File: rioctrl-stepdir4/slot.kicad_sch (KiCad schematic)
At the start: 17 parts, among them J1 Conn_02x13_Odd_Even, Q1 BSS138W, Q2 BSS138W, Q3 AO3401A, Q4 AO3401A

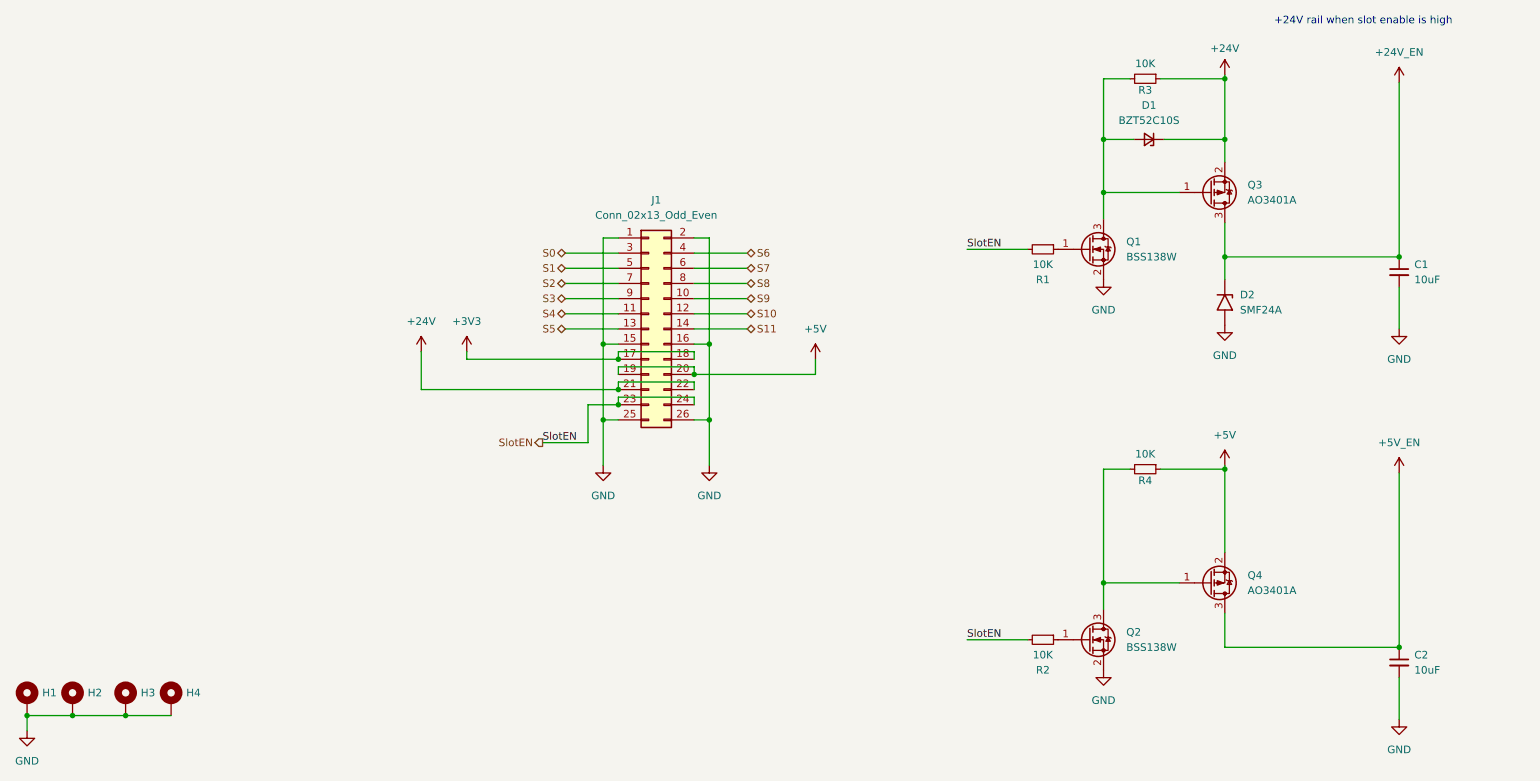
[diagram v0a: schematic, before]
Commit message: rioctrl-stepdir4: pass ERC and DRC
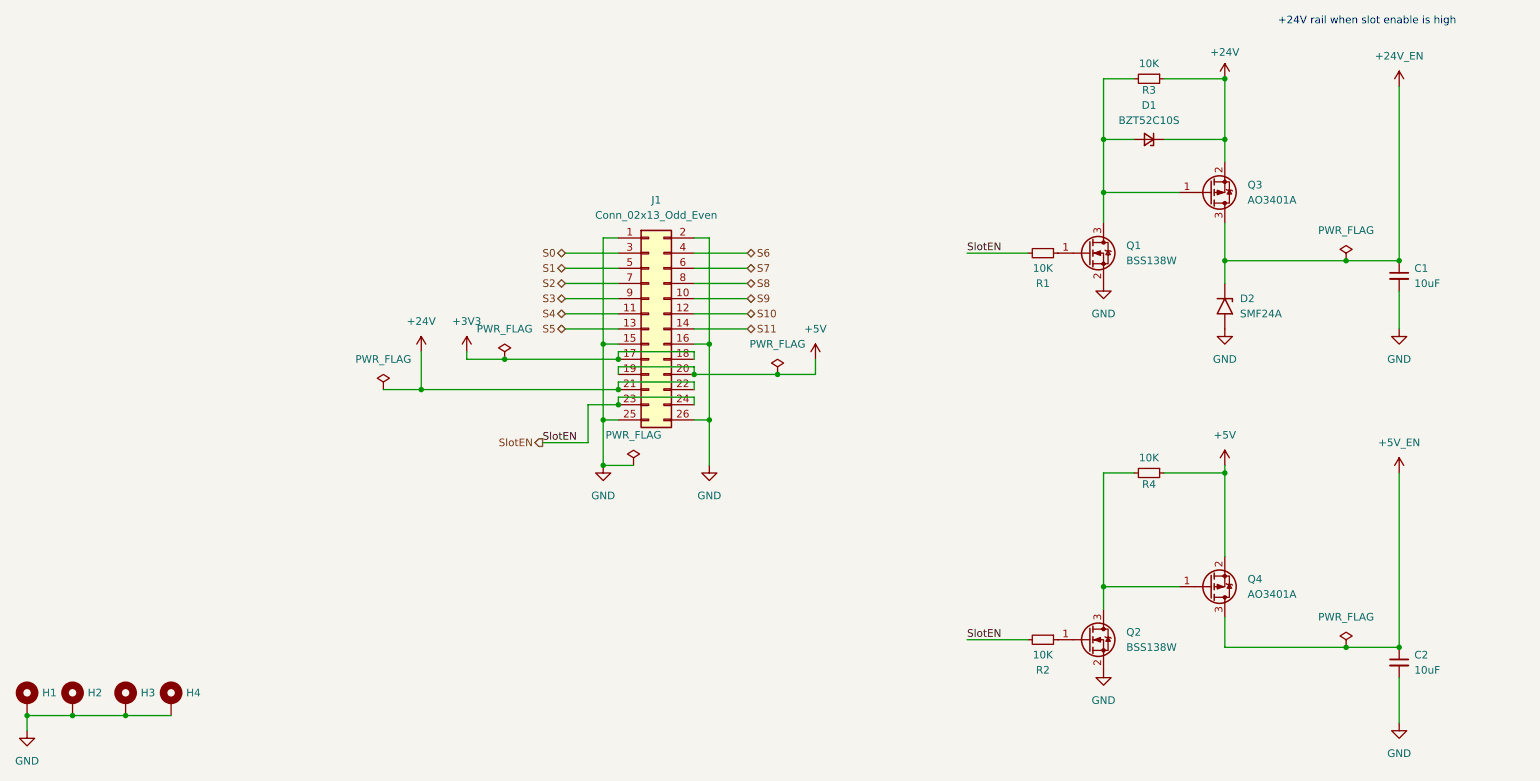
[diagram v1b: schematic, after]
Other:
- moved on the sheet: C1, D2, Q1, Q4, R1, R3, R4

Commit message: Fix ERC, add title information to sch, add initial version of build scripts
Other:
- company: (none) -> R. Veips
- title: (none) -> rioctrl-stepdir4
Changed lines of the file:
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@@
 	(generator_version "8.0")
 	(paper "A4")
+	(title_block
+		(title "rioctrl-stepdir4")
+		(date "2024-08-25")
+		(rev "${VERSION}")
+		(company "R. Veips")
+	)
 	(junction
 		(at 213.36 118.11)

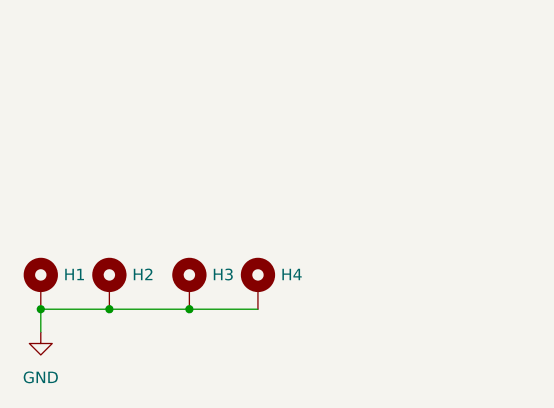
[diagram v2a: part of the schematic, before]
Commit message: Fill in BOM (LCSC#)
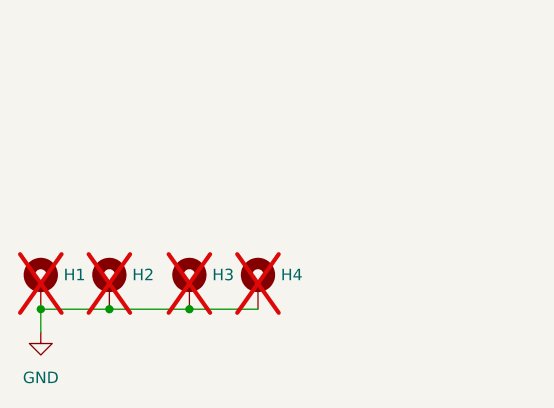
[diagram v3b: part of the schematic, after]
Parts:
- H1, H2, H3, H4: now not fitted
- J1: LCSC# (none) -> C2894993
- R1, R2, R3, R4: LCSC# (none) -> C98220
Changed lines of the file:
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@@
 		(in_bom no)
 		(on_board yes)
-		(dnp no)
+		(dnp yes)
 		(fields_autoplaced yes)
 		(property "Reference" "H4"
@@
 		(in_bom no)
 		(on_board yes)
-		(dnp no)
+		(dnp yes)
 		(fields_autoplaced yes)
 		(property "Reference" "H1"
@@
 			)
 		)
+		(property "LCSC#" "C2894993"
+			(at 137.16 74.93 0)
+			(effects
+				(font
+					(size 1.27 1.27)
+				)
+				(hide yes)
+			)
+		)
 		(pin "15"
 		)
@@
 			)
 		)
+		(property "LCSC#" "C98220"
+			(at 203.2 127 0)
+			(effects
+				(font
+					(size 1.27 1.27)
+				)
+				(hide yes)
+			)
+		)
 		(pin "1"
 		)
@@
 			)
 		)
+		(property "LCSC#" "C98220"
+			(at 220.98 33.02 0)
+			(effects
+				(font
+					(size 1.27 1.27)
+				)
+				(hide yes)
+			)
+		)
 		(pin "1"
 		)
@@
 		)
 		(property "Description" ""
+			(at 220.98 99.06 0)
+			(effects
+				(font
+					(size 1.27 1.27)
+				)
+				(hide yes)
+			)
+		)
+		(property "LCSC#" "C98220"
 			(at 220.98 99.06 0)
 			(effects
@@
 			)
 		)
+		(property "LCSC#" "C98220"
+			(at 203.2 62.23 0)
+			(effects
+				(font
+					(size 1.27 1.27)
+				)
+				(hide yes)
+			)
+		)
 		(pin "1"
 		)
@@
 		(in_bom no)
 		(on_board yes)
-		(dnp no)
+		(dnp yes)
 		(fields_autoplaced yes)
 		(property "Reference" "H3"
@@
 		(in_bom no)
 		(on_board yes)
-		(dnp no)
+		(dnp yes)
 		(fields_autoplaced yes)
 		(property "Reference" "H2"

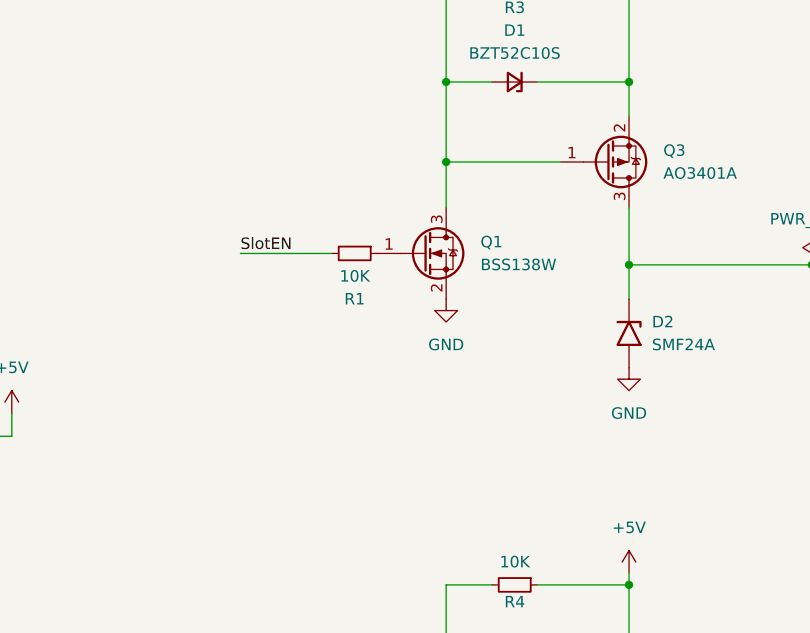
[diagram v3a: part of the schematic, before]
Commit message: Add forgotten series resistor for 24V output transistors in rioctrl-stepdir4
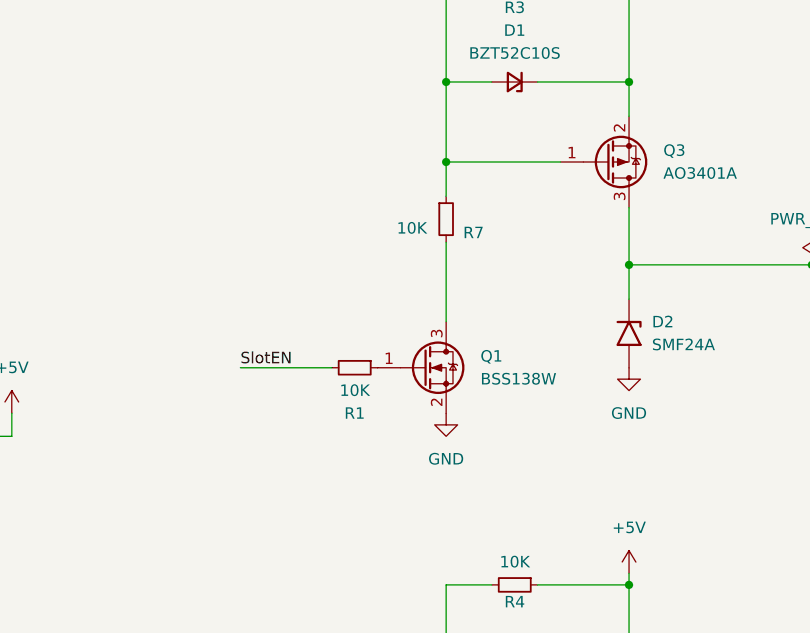
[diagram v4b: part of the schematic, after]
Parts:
- added R7: 10K, Resistor_SMD:R_0603_1608Metric, symbol Device:R_Small
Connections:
- net at D1.2 (A), Q3.1 (G), R3.2: now also R7.1; no longer Q1.3 (D)
- new net: Q1.3 (D), R7.2
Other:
- moved on the sheet: Q1, R1
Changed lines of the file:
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@@
 	(wire
 		(pts
-			(xy 190.5 62.23) (xy 200.66 62.23)
+			(xy 190.5 74.93) (xy 200.66 74.93)
 		)
 		(stroke
@@
 	(wire
 		(pts
-			(xy 213.36 52.07) (xy 213.36 57.15)
+			(xy 213.36 52.07) (xy 213.36 55.88)
 		)
 		(stroke
@@
 		(pts
 			(xy 158.75 82.55) (xy 165.1 82.55)
+		)
+		(stroke
+			(width 0)
+			(type default)
+		)
+	)
+	(wire
+		(pts
+			(xy 213.36 60.96) (xy 213.36 69.85)
 		)
 		(stroke
@@
 	)
 	(label "SlotEN"
-		(at 190.5 62.23 0)
+		(at 190.5 74.93 0)
 		(fields_autoplaced yes)
 		(effects
@@
 	(symbol
 		(lib_id "hadv-transistors:BSS138W")
-		(at 210.82 62.23 0)
+		(at 210.82 74.93 0)
 		(unit 1)
 		(exclude_from_sim no)
@@
 		(fields_autoplaced yes)
 		(property "Reference" "Q1"
-			(at 217.17 60.96 0)
+			(at 217.17 73.66 0)
 			(effects
 				(font
@@
 		)
 		(property "Value" "BSS138W"
-			(at 217.17 63.5 0)
+			(at 217.17 76.2 0)
 			(effects
 				(font
@@
 		)
 		(property "Footprint" "Package_TO_SOT_SMD:SOT-323_SC-70"
-			(at 215.9 59.69 0)
+			(at 215.9 72.39 0)
 			(effects
 				(font
@@
 		)
 		(property "Datasheet" "~"
-			(at 210.82 62.23 0)
+			(at 210.82 74.93 0)
 			(effects
 				(font
@@
 		)
 		(property "Description" ""
-			(at 210.82 62.23 0)
+			(at 210.82 74.93 0)
 			(effects
 				(font
@@
 		)
 		(property "MPN" "BSS138W"
-			(at 210.82 62.23 0)
+			(at 210.82 74.93 0)
 			(effects
 				(font
@@
 		)
 		(property "Manufacturer" "Jiangsu Changjing Electronics Technology Co., Ltd."
-			(at 210.82 62.23 0)
+			(at 210.82 74.93 0)
 			(effects
 				(font
@@
 		)
 		(property "LCSC#" "C504052"
-			(at 210.82 62.23 0)
+			(at 210.82 74.93 0)
 			(effects
 				(font
@@
 	(symbol
 		(lib_id "power:GND")
-		(at 213.36 67.31 0)
+		(at 213.36 80.01 0)
 		(unit 1)
 		(exclude_from_sim no)
@@
 		(fields_autoplaced yes)
 		(property "Reference" "#PWR06"
-			(at 213.36 73.66 0)
+			(at 213.36 86.36 0)
 			(effects
 				(font
@@
 		)
 		(property "Value" "GND"
-			(at 213.36 72.39 0)
+			(at 213.36 85.09 0)
 			(effects
 				(font
@@
 		)
 		(property "Footprint" ""
-			(at 213.36 67.31 0)
+			(at 213.36 80.01 0)
 			(effects
 				(font
@@
 		)
 		(property "Datasheet" ""
-			(at 213.36 67.31 0)
+			(at 213.36 80.01 0)
 			(effects
 				(font
@@
 		)
 		(property "Description" "Power symbol creates a global label with name \"GND\" , ground"
-			(at 213.36 67.31 0)
+			(at 213.36 80.01 0)
 			(effects
 				(font
@@
 				(path "/09587842-9628-4761-8ca3-5c7cdb77bd67/37e028e8-dcad-4a75-b244-5f607e32f85e"
 					(reference "#PWR06")
+					(unit 1)
+				)
+			)
+		)
+	)
+	(symbol
+		(lib_id "Device:R_Small")
+		(at 213.36 58.42 0)
+		(unit 1)
+		(exclude_from_sim no)
+		(in_bom yes)
+		(on_board yes)
+		(dnp no)
+		(property "Reference" "R7"
+			(at 216.408 59.944 0)
+			(effects
+				(font
+					(size 1.27 1.27)
+				)
+			)
+		)
+		(property "Value" "10K"
+			(at 209.55 59.436 0)
+			(effects
+				(font
+					(size 1.27 1.27)
+				)
+			)
+		)
+		(property "Footprint" "Resistor_SMD:R_0603_1608Metric"
+			(at 213.36 58.42 0)
+			(effects
+				(font
+					(size 1.27 1.27)
+				)
+				(hide yes)
+			)
+		)
+		(property "Datasheet" "~"
+			(at 213.36 58.42 0)
+			(effects
+				(font
+					(size 1.27 1.27)
+				)
+				(hide yes)
+			)
+		)
+		(property "Description" ""
+			(at 213.36 58.42 0)
+			(effects
+				(font
+					(size 1.27 1.27)
+				)
+				(hide yes)
+			)
+		)
+		(property "LCSC#" "C98220"
+			(at 213.36 58.42 0)
+			(effects
+				(font
+					(size 1.27 1.27)
+				)
+				(hide yes)
+			)
+		)
+		(pin "1"
+		)
+		(pin "2"
+		)
+		(instances
+			(project "rioctrl-stepdir4"
+				(path "/09587842-9628-4761-8ca3-5c7cdb77bd67/37e028e8-dcad-4a75-b244-5f607e32f85e"
+					(reference "R7")
 					(unit 1)
 				)
@@
 	(symbol
 		(lib_id "Device:R_Small")
-		(at 203.2 62.23 270)
+		(at 203.2 74.93 270)
 		(unit 1)
 		(exclude_from_sim no)
@@
 		(dnp no)
 		(property "Reference" "R1"
-			(at 203.2 67.31 90)
+			(at 203.2 80.01 90)
 			(effects
 				(font
@@
 		)
 		(property "Value" "10K"
-			(at 203.2 64.77 90)
+			(at 203.2 77.47 90)
 			(effects
 				(font
@@
 		)
 		(property "Footprint" "Resistor_SMD:R_0603_1608Metric"
-			(at 203.2 62.23 0)
+			(at 203.2 74.93 0)
 			(effects
 				(font
@@
 		)
 		(property "Datasheet" "~"
-			(at 203.2 62.23 0)
+			(at 203.2 74.93 0)
 			(effects
 				(font
@@
 		)
 		(property "Description" ""
-			(at 203.2 62.23 0)
+			(at 203.2 74.93 0)
 			(effects
 				(font
@@
 		)
 		(property "LCSC#" "C98220"
-			(at 203.2 62.23 0)
-			(effects
-				(font
+			(at 203.2 74.93 0)
+			(effects
+				(font
